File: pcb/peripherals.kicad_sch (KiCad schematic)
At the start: 51 parts, among them U4 MCP23017T-E/ML

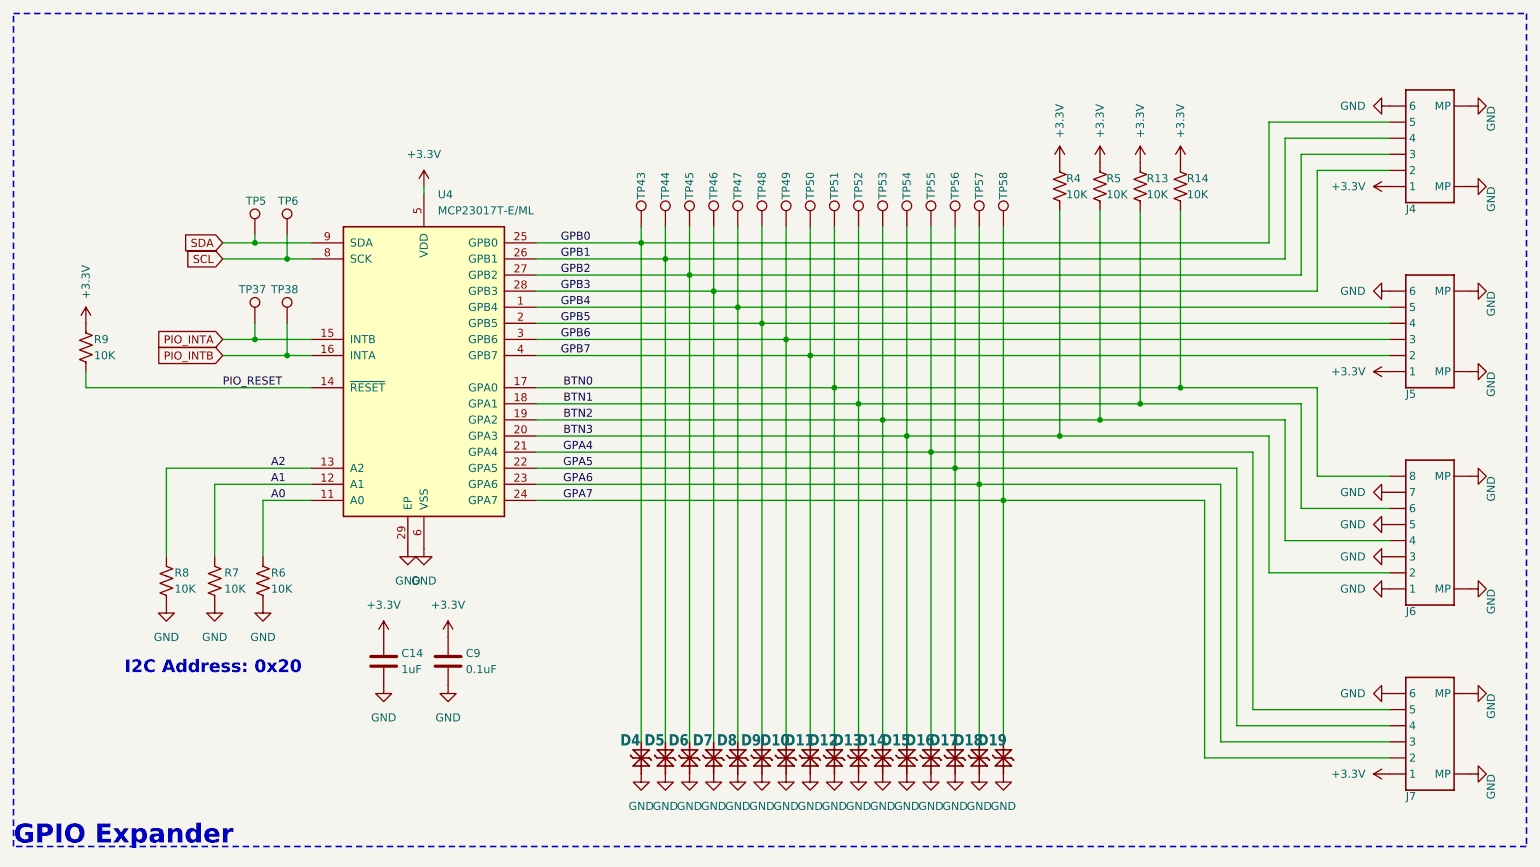
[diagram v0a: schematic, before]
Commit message: Renamed and added guard ring
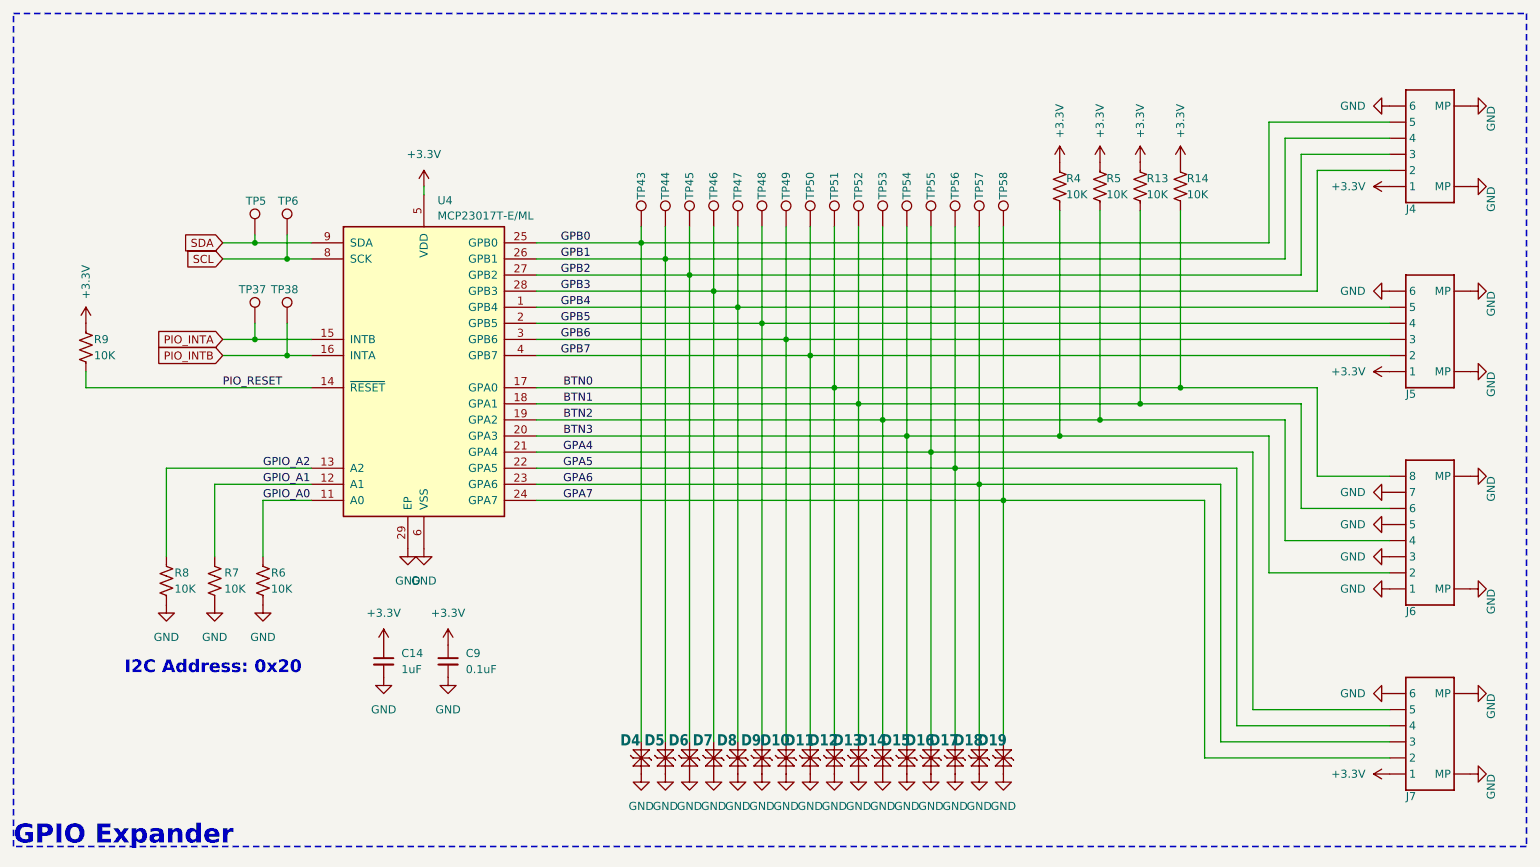
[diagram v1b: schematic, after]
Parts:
- C14, C9: symbol Device:C -> CRGM Passive:C_Small
- J4, J5, J6, J7, TP37, TP38, TP43, TP44, TP45, TP46, TP47, TP48, TP49, TP5, TP50, TP51, TP52, TP53, TP54, TP55, TP56, TP57, TP58, TP6: value ~ -> (none)
- U4: symbol Interface_Expansion:MCP23017_ML -> CRG Makes:MCP23017_ML
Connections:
- net A0 renamed GPIO_A0
- net A1 renamed GPIO_A1
- net A2 renamed GPIO_A2
